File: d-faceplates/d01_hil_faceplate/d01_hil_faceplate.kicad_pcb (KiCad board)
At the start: 2 copper layers, 23.8 x 64 mm, 12 parts

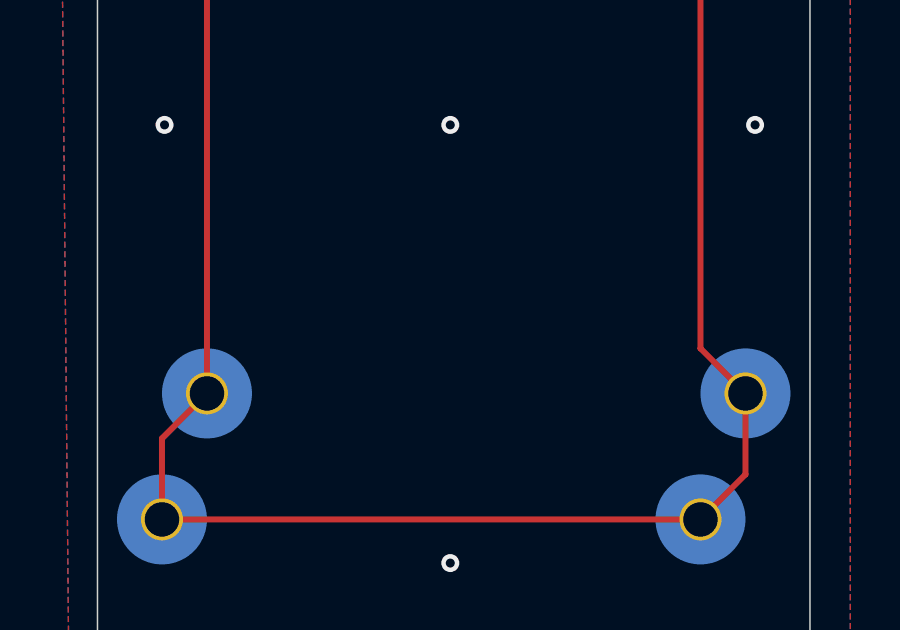
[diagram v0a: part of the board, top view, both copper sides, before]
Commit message: d01_hil_faceplate: add single-board Gerber outputs
Export gerber/single (copper, mask, paste, silkscreen, edge cuts, drills, and d01-hil-faceplate-single.zip), refresh PCB and fp-info-cache, and rotate KiCad automatic backup.
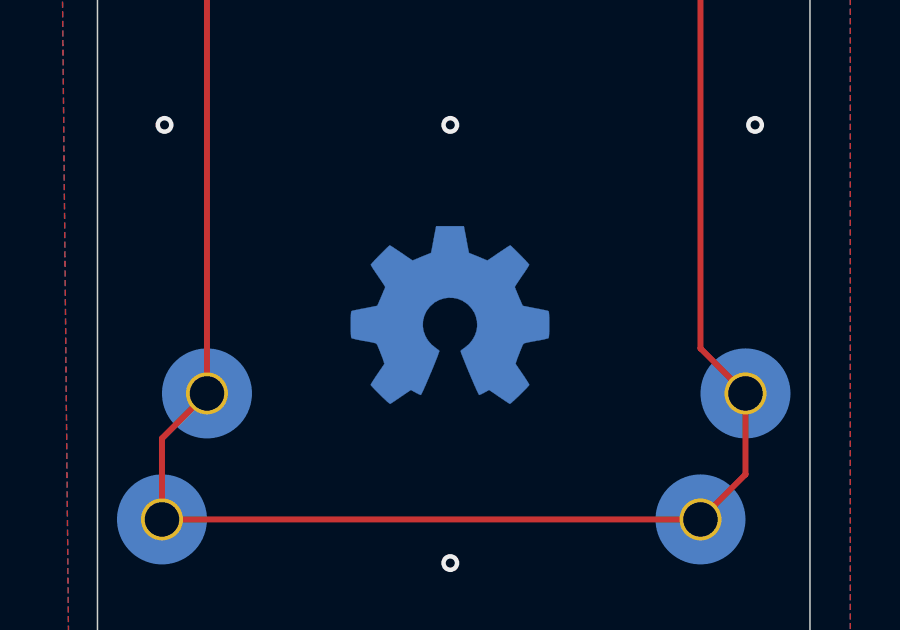
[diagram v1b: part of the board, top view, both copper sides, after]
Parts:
- added REF**: OSHW-Symbol_6.7x6mm_Copper, Symbol:OSHW-Symbol_6.7x6mm_Copper, B.Cu at (111.8, 152.4)
